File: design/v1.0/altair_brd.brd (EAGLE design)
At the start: 91.4 x 68.9 mm, 68 parts, among them J1 TYPE-C-31-M-12, J2 USB-A-S-X-X-TH, J3 22-03-5035, J4 22-03-5035, J5 22-03-5035, J6 22-03-5035, J7 22-03-5035, Q1 IRF9540, Q10 NPN, Q2 IRF9540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

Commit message: Version fixed
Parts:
- added S1, S2: MOMENTARY-SWITCH-SPST-SMD-6.2MM-TALL, SparkFun-Switches:TACTILE_SWITCH_SMD_6.2MM_TALL
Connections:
- net ESP_EN: now also S1.A2
- net ESP_IO0: now also S2.A2
- net GND: now also S1.B2, S2.B2
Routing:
- net ESP_EN: track 46.3 -> 84.5 mm, vias 3 -> 4
- net ESP_IO0: track 9.87 -> 46.3 mm, vias 0 -> 1
- net VBAT: track 211.6 -> 231.1 mm
- net 3V3: track 90.6 -> 92.7 mm
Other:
- board text added: "BOOT"
- board text added: "EN / RST"

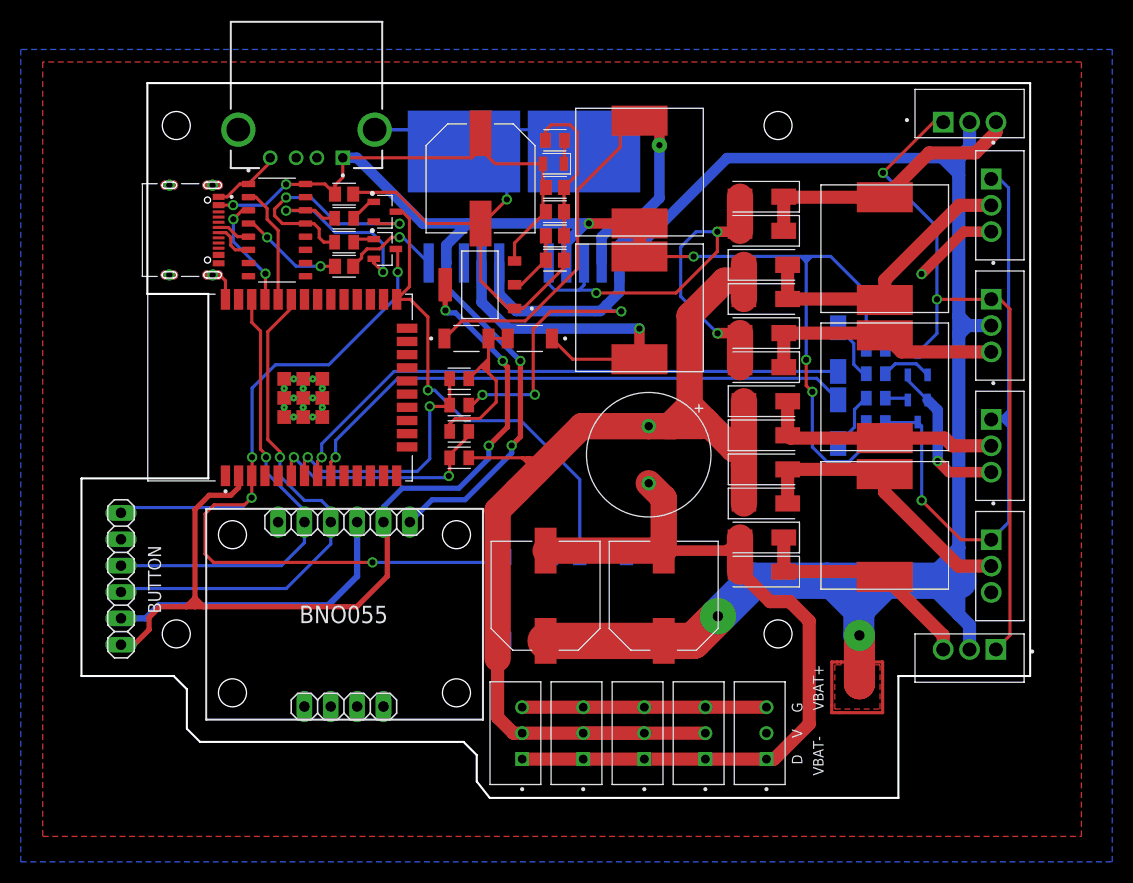
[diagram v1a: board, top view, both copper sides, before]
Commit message: Button interrupt added
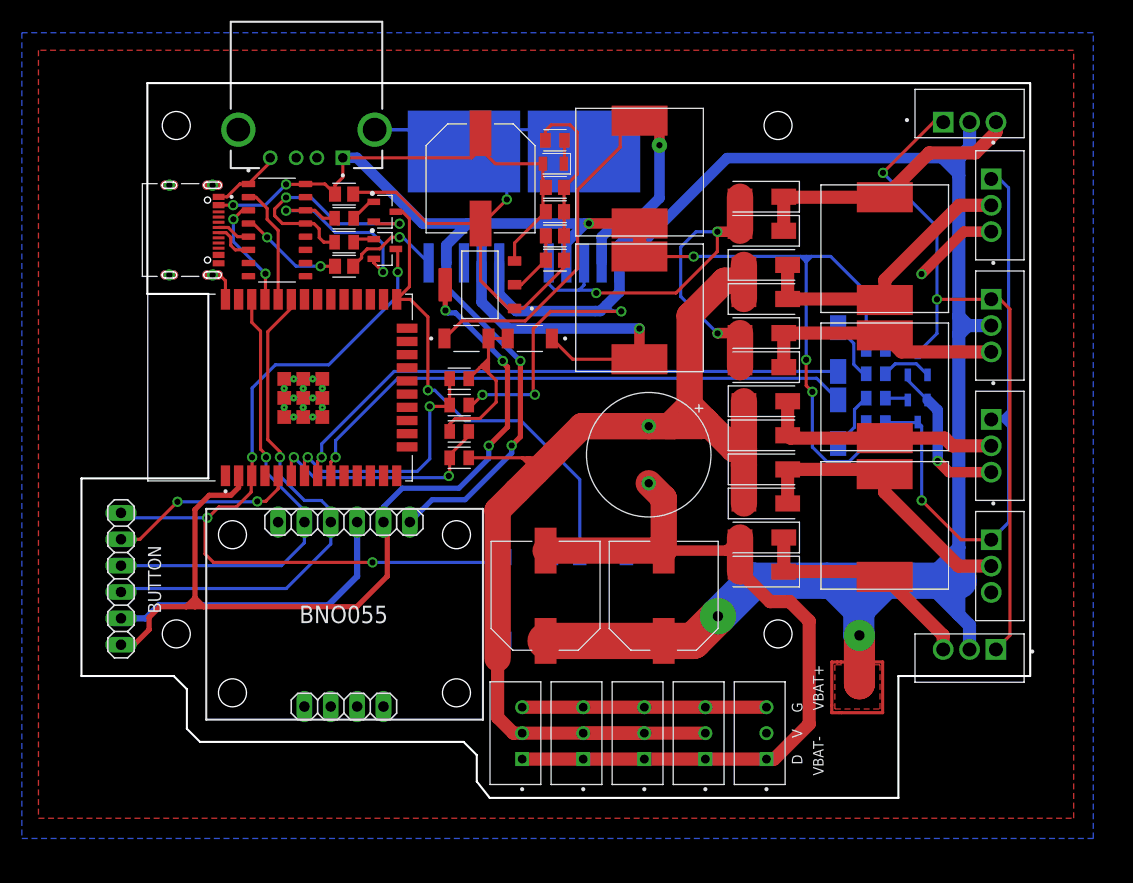
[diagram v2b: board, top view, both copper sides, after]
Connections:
- net BTN_INT: now also U1.5
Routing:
- net BTN_INT: track 0.00 -> 18.4 mm, vias 0 -> 2
- net ESP_EN: track 84.5 -> 79.2 mm
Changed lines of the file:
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@@
 <contactref element="S1" pad="B2"/>
 <contactref element="S2" pad="B2"/>
-<polygon width="0.3048" layer="1" spacing="1.27" pour="solid" isolate="0.4064" thermals="yes">
-<vertex x="-3.70331875" y="-15.43811875"/>
-<vertex x="96.408240625" y="-15.43811875"/>
-<vertex x="96.408240625" y="59.2074"/>
-<vertex x="-3.70331875" y="59.2074"/>
+<polygon width="0.3048" layer="1" spacing="1.27" pour="solid" isolate="0.3048" thermals="yes">
+<vertex x="-4.1148" y="-13.68551875"/>
+<vertex x="95.66148125" y="-13.68551875"/>
+<vertex x="95.66148125" y="60.335159375"/>
+<vertex x="-4.1148" y="60.335159375"/>
 </polygon>
-<polygon width="0.3048" layer="16" spacing="1.27" pour="solid" isolate="0.4064" thermals="yes">
-<vertex x="-5.82168125" y="-17.891759375"/>
-<vertex x="99.380040625" y="-17.891759375"/>
-<vertex x="99.380040625" y="60.411359375"/>
-<vertex x="-5.82168125" y="60.411359375"/>
+<polygon width="0.3048" layer="16" spacing="1.27" pour="solid" isolate="0.3048" thermals="yes">
+<vertex x="-5.715" y="-15.636240625"/>
+<vertex x="97.551240625" y="-15.636240625"/>
+<vertex x="97.551240625" y="62.0268"/>
+<vertex x="-5.715" y="62.0268"/>
 </polygon>
 <wire x1="21.40706875" y1="25.905540625" x2="21.40706875" y2="26.823040625" width="0" layer="19" extent="1-1"/>
@@
 <contactref element="JP3" pad="4"/>
 <wire x1="3.840478125" y1="10.65941875" x2="19.3084875" y2="10.65941875" width="0.3048" layer="16"/>
-<wire x1="19.3084875" y1="10.65941875" x2="21.51990625" y2="12.8708375" width="0.3048" layer="16"/>
-<wire x1="21.51990625" y1="12.8708375" x2="21.51990625" y2="14.861496875" width="0.3048" layer="16"/>
+<wire x1="21.51990625" y1="12.8708375" x2="19.3084875" y2="10.65941875" width="0.3048" layer="16"/>
+<wire x1="21.51990625" y1="14.861496875" x2="21.51990625" y2="12.8708375" width="0.3048" layer="16"/>
 <wire x1="16.44706875" y1="36.323040625" x2="16.44706875" y2="34.1055" width="0.3048" layer="1"/>
 <wire x1="16.44706875" y1="34.1055" x2="17.29070625" y2="33.2618625" width="0.3048" layer="1"/>
@@
 <wire x1="16.477534375" y1="19.35350625" x2="16.44706875" y2="19.323040625" width="0.3048" layer="1"/>
 <contactref element="JP3" pad="6"/>
-<wire x1="16.44706875" y1="19.323040625" x2="16.44706875" y2="17.218653125" width="0.3048" layer="1"/>
-<wire x1="16.44706875" y1="17.218653125" x2="16.431184375" y2="17.20276875" width="0.3048" layer="1"/>
-<via x="16.431184375" y="17.20276875" extent="1-16" drill="0.6">
-</via>
-<wire x1="16.431184375" y1="17.20276875" x2="15.48608125" y2="16.257665625" width="0.3048" layer="16"/>
-<wire x1="15.48608125" y1="16.257665625" x2="4.358725" y2="16.257665625" width="0.3048" layer="16"/>
-<wire x1="4.358725" y1="16.257665625" x2="3.840478125" y2="15.73941875" width="0.3048" layer="16"/>
+<via x="12.1567625" y="15.27188125" extent="1-16" drill="0.6">
+</via>
 <contactref element="S1" pad="A2"/>
-<wire x1="16.431184375" y1="17.20276875" x2="15.75421875" y2="16.525803125" width="0.3048" layer="1"/>
-<wire x1="15.75421875" y1="16.525803125" x2="12.823259375" y2="16.525803125" width="0.3048" layer="1"/>
-<wire x1="12.823259375" y1="16.525803125" x2="11.938890625" y2="15.641434375" width="0.3048" layer="1"/>
-<wire x1="11.938890625" y1="15.641434375" x2="11.938890625" y2="11.790409375" width="0.3048" layer="1"/>
 <wire x1="11.938890625" y1="11.790409375" x2="12.75609375" y2="10.97320625" width="0.3048" layer="1"/>
 <wire x1="12.75609375" y1="10.97320625" x2="28.0817625" y2="10.97320625" width="0.3048" layer="1"/>
@@
 <wire x1="28.0817625" y1="10.97320625" x2="40.33359375" y2="10.97320625" width="0.3048" layer="16"/>
 <wire x1="40.33359375" y1="10.97320625" x2="40.833471875" y2="11.473084375" width="0.3048" layer="16"/>
+<wire x1="14.961990625" y1="16.317475" x2="13.27513125" y2="16.317475" width="0.3048" layer="1"/>
+<wire x1="13.27513125" y1="16.317475" x2="12.193153125" y2="15.235496875" width="0.3048" layer="1"/>
+<wire x1="16.44706875" y1="19.323040625" x2="16.390121875" y2="19.26609375" width="0.3048" layer="1"/>
+<wire x1="16.390121875" y1="19.26609375" x2="16.390121875" y2="17.74560625" width="0.3048" layer="1"/>
+<wire x1="16.390121875" y1="17.74560625" x2="14.961990625" y2="16.317475" width="0.3048" layer="1"/>
+<wire x1="11.938890625" y1="14.981234375" x2="11.938890625" y2="11.790409375" width="0.3048" layer="1"/>
+<wire x1="12.193153125" y1="15.235496875" x2="12.193153125" y2="15.235490625" width="0.3048" layer="1"/>
+<wire x1="12.193153125" y1="15.235490625" x2="12.1567625" y2="15.27188125" width="0.3048" layer="1"/>
+<wire x1="12.193153125" y1="15.235496875" x2="11.938890625" y2="14.981234375" width="0.3048" layer="1"/>
+<wire x1="3.840478125" y1="15.73941875" x2="4.308015625" y2="15.27188125" width="0.3048" layer="16"/>
+<wire x1="4.308015625" y1="15.27188125" x2="12.1567625" y2="15.27188125" width="0.3048" layer="16"/>
 </signal>
 <signal name="ESP_IO0">
@@
 <signal name="BTN_INT">
 <contactref element="JP3" pad="5"/>
+<contactref element="U1" pad="5"/>
+<wire x1="3.840478125" y1="13.19941875" x2="5.668303125" y2="13.19941875" width="0.3048" layer="1"/>
+<wire x1="5.668303125" y1="13.19941875" x2="9.282903125" y2="16.81401875" width="0.3048" layer="1"/>
+<via x="9.282903125" y="16.81401875" extent="1-16" drill="0.6">
+</via>
+<wire x1="9.282903125" y1="16.81401875" x2="16.9370625" y2="16.81401875" width="0.3048" layer="16"/>
+<wire x1="16.9370625" y1="16.81401875" x2="16.978521875" y2="16.855478125" width="0.3048" layer="16"/>
+<via x="16.978521875" y="16.855478125" extent="1-16" drill="0.6">
+</via>
+<wire x1="17.81150625" y1="16.855478125" x2="16.978521875" y2="16.855478125" width="0.3048" layer="1"/>
+<wire x1="18.98706875" y1="19.323040625" x2="18.98706875" y2="18.069059375" width="0.3048" layer="1"/>
+<wire x1="18.98706875" y1="18.069059375" x2="17.81150625" y2="16.893496875" width="0.3048" layer="1"/>
+<wire x1="17.81150625" y1="16.855478125" x2="17.81150625" y2="16.893496875" width="0" layer="19" extent="1-1"/>
 </signal>
 <signal name="DATA">
